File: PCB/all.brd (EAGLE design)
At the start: 45 x 45 mm, 119 parts, among them J1 ISP Programmer, J2 LIPO-BATTERY-CONNECTOR, J8 BL-HP20AUW2C, U1 ATTINY1634MLF20, U2 LM3671, U3 MPU-6050-1, U4 BQ51013B_RHL_20, U5 MCP73831, U6 CAT4139, U7 BQ51013B_RHL_20, U8 BQ51013B_RHL_20, U9 BQ51013B_RHL_20

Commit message: Component placement
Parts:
- moved R6 87.2 mm to (2.29, 24.7), turned to 90 degrees
- moved J2 84.2 mm to (4.37, 19.7), turned to 270 degrees
- moved U5 83.2 mm to (4.33, 24.3), turned to 0 degrees
- moved L2 77.9 mm to (21.6, 37.8), turned to 180 degrees
- moved C15 77.5 mm to (7.28, 23.1), turned to 90 degrees
- moved C12 74.8 mm to (11.4, 23.6), turned to 270 degrees
- moved R19 74.8 mm to (17.4, 11.8), turned to 90 degrees
- moved C10 74.8 mm to (15.2, 26.7), turned to 0 degrees
- moved R18 74.2 mm to (15.5, 14.9), turned to 90 degrees
- moved U2 73.5 mm to (22.0, 34.1), turned to 270 degrees
- moved R20 72.5 mm to (18.9, 11.8), turned to 270 degrees
- moved C13 72.5 mm to (17.4, 26.3), turned to 90 degrees
- moved C8 71.6 mm to (21.8, 32.0), turned to 0 degrees
- moved L1 71.4 mm to (23.8, 7.85), turned to 0 degrees
- moved U3 71.1 mm to (14.6, 22.9), turned to 180 degrees
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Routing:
- net RGB: track 0.00 -> 5.78 mm
- net 5V: track 5.39 -> 8.41 mm
- net N$15: track 0.00 -> 2.55 mm
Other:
- board text added: "Board layout 26.7.2016"
- board text added: "www.helentronica.com"
- board text removed: "Prelimirary board layout 26.7.2016"

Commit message: routing finished
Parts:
- C1, C17, C20, C22, C25, C28, C5, CP1, CP2, CP3, CP4, CP5, CP6, CP7, CP8, CS, CS1, CS10, CS11, CS12, CS13, CS14, CS15, CS16, CS17, CS19, CS2, CS20, CS21, CS22, CS23, CS24, CS25, CS26, CS27, CS28, CS29, CS3, CS30, CS31, CS32, CS33, CS34, CS35, CS36, CS37, CS38, CS39, CS4, CS5, CS6, CS7, CS8, CS9: device rcl:C0603 -> rcl:C0603K
- C10, C11, C12, C6, C7, C8, C9: device rcl:C0402 -> rcl:C0603K
- C13: device SparkFun:0603-CAP -> rcl:C0603K
- moved D2 4.85 mm to (8.58, 15.9)
- moved C1 3.25 mm to (17.2, 11.8)
- moved U5 1.97 mm to (5.93, 23.2)
- moved J2 1.51 mm to (4.57, 18.2)
- moved C15 1.35 mm to (8.63, 23.1)
- moved C14 1.25 mm to (36.3, 24.3)
- moved JP2 1.25 mm to (39.3, 20.5)
- moved R19 1.25 mm to (18.6, 11.8)
- moved R20 1.25 mm to (20.1, 11.8)
- moved R5 1.25 mm to (35.9, 20.5)
- moved R6 0.91 mm to (2.84, 25.4), turned to 0 degrees
- moved C5 0.88 mm to (24.1, 30.6)
- moved R1 0.46 mm to (26.3, 29.5)
- moved R15 0.35 mm to (8.15, 42.6)
- moved R4 0.35 mm to (42.6, 36.9)
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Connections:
- removed net VBAT: J2.P$1, U5.3
- net 5V: now also J2.P$1, U5.3
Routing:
- net V_QI_IN: track 3.32 -> 85.2 mm
- net 5V: track 8.41 -> 86.0 mm, vias 0 -> 3
- net 3.3V: track 23.8 -> 49.6 mm
- net SCL: track 6.12 -> 22.7 mm
- net N$18: track 0.00 -> 13.0 mm, vias 0 -> 2
- net PWM: track 0.00 -> 12.8 mm, vias 0 -> 1
- net N$64: track 0.00 -> 8.11 mm, vias 0 -> 1
- net SDA: track 13.2 -> 21.1 mm, vias 0 -> 1
- net N$2: track 0.00 -> 7.85 mm
- net N$63: track 0.00 -> 5.68 mm
- net N$65: track 0.00 -> 5.63 mm
- net N$3: track 0.00 -> 4.40 mm, vias 0 -> 1
- net RST: track 3.09 -> 7.10 mm
- net N$62: track 0.00 -> 3.49 mm
- net VBAT: track 2.66 -> 0.00 mm
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
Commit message: DRC done
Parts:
- added DRILEGEND: (no value), drilegend:DRILEGEND
- J3, J4, J5, J6: value (none) -> Qi coil
- J7: value (none) -> UART
- Q1, Q2: value (none) -> NPN
- R18: value (none) -> 1.8
- moved C11 0.78 mm to (13.5, 19.0)
- moved C8 0.46 mm to (21.6, 31.6)
- moved U2 0.20 mm to (22.0, 33.9)
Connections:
- net 5V renamed +5V
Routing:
- net GND: track 9.08 -> 67.8 mm, vias 2 -> 47
- net V_QI3: track 12.3 -> 14.2 mm
- net V_QI_IN: track 85.2 -> 86.5 mm
- net 3.3V: track 49.6 -> 50.6 mm
- net N$1: track 1.59 -> 2.37 mm

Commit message: gerber generated
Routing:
- net GND: vias 47 -> 49
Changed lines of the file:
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@@
 <layer number="14" name="Route14" color="1" fill="6" visible="no" active="no"/>
 <layer number="15" name="Route15" color="4" fill="6" visible="no" active="no"/>
-<layer number="16" name="Bottom" color="1" fill="1" visible="yes" active="yes"/>
+<layer number="16" name="Bottom" color="1" fill="1" visible="no" active="yes"/>
 <layer number="17" name="Pads" color="2" fill="1" visible="yes" active="yes"/>
 <layer number="18" name="Vias" color="2" fill="1" visible="yes" active="yes"/>
-<layer number="19" name="Unrouted" color="6" fill="1" visible="yes" active="yes"/>
+<layer number="19" name="Unrouted" color="6" fill="1" visible="no" active="yes"/>
 <layer number="20" name="Dimension" color="15" fill="1" visible="yes" active="yes"/>
 <layer number="21" name="tPlace" color="7" fill="1" visible="yes" active="yes"/>
-<layer number="22" name="bPlace" color="7" fill="1" visible="yes" active="yes"/>
+<layer number="22" name="bPlace" color="7" fill="1" visible="no" active="yes"/>
 <layer number="23" name="tOrigins" color="15" fill="1" visible="no" active="yes"/>
 <layer number="24" name="bOrigins" color="15" fill="1" visible="no" active="yes"/>
-<layer number="25" name="tNames" color="7" fill="1" visible="no" active="yes"/>
+<layer number="25" name="tNames" color="7" fill="1" visible="yes" active="yes"/>
 <layer number="26" name="bNames" color="7" fill="1" visible="no" active="yes"/>
 <layer number="27" name="tValues" color="7" fill="1" visible="no" active="yes"/>
 <layer number="28" name="bValues" color="7" fill="1" visible="no" active="yes"/>
-<layer number="29" name="tStop" color="7" fill="3" visible="no" active="yes"/>
+<layer number="29" name="tStop" color="7" fill="3" visible="yes" active="yes"/>
 <layer number="30" name="bStop" color="7" fill="6" visible="no" active="yes"/>
 <layer number="31" name="tCream" color="7" fill="4" visible="no" active="yes"/>
@@
 <layer number="39" name="tKeepout" color="4" fill="11" visible="no" active="yes"/>
 <layer number="40" name="bKeepout" color="1" fill="11" visible="no" active="yes"/>
-<layer number="41" name="tRestrict" color="4" fill="10" visible="yes" active="yes"/>
-<layer number="42" name="bRestrict" color="1" fill="10" visible="yes" active="yes"/>
+<layer number="41" name="tRestrict" color="4" fill="10" visible="no" active="yes"/>
+<layer number="42" name="bRestrict" color="1" fill="10" visible="no" active="yes"/>
 <layer number="43" name="vRestrict" color="2" fill="10" visible="no" active="yes"/>
 <layer number="44" name="Drills" color="7" fill="1" visible="no" active="yes"/>
 <layer number="45" name="Holes" color="7" fill="1" visible="no" active="yes"/>
 <layer number="46" name="Milling" color="3" fill="1" visible="no" active="yes"/>
-<layer number="47" name="Measures" color="7" fill="1" visible="yes" active="yes"/>
-<layer number="48" name="Document" color="7" fill="1" visible="yes" active="yes"/>
+<layer number="47" name="Measures" color="7" fill="1" visible="no" active="yes"/>
+<layer number="48" name="Document" color="7" fill="1" visible="no" active="yes"/>
 <layer number="49" name="Reference" color="7" fill="1" visible="no" active="yes"/>
 <layer number="50" name="dxf" color="7" fill="1" visible="no" active="no"/>
@@
 <layer number="131" name="tAdjust" color="7" fill="1" visible="no" active="yes"/>
 <layer number="132" name="bAdjust" color="7" fill="1" visible="no" active="yes"/>
-<layer number="144" name="DrillLegend" color="7" fill="1" visible="yes" active="yes"/>
+<layer number="144" name="DrillLegend" color="7" fill="1" visible="no" active="yes"/>
 <layer number="145" name="DrillLegend_01-16" color="2" fill="9" visible="no" active="yes"/>
 <layer number="146" name="DrillLegend_01-20" color="3" fill="9" visible="no" active="yes"/>
@@
 <text x="110" y="-55" size="2.54" layer="48">Pero</text>
 <text x="110" y="-60" size="2.54" layer="48">July, 2016</text>
-<dimension x1="40" y1="5" x2="40" y2="0" x3="40" y3="2.5" textsize="2.54" layer="47" dtype="vertical" extoffset="1" visible="yes"/>
 <text x="60" y="-55" size="2.54" layer="48">Board layout
 26.7.2016</text>
@@
 <text x="42.5" y="33.75" size="2.54" layer="26" rot="MR0">www.helentronica.com</text>
 <dimension x1="0" y1="45" x2="22.5" y2="42.5" x3="11.25" y3="48.75" textsize="2.54" layer="47" dtype="horizontal" visible="yes"/>
-<dimension x1="0" y1="0" x2="22.5" y2="2.5" x3="11.25" y3="-5.6" textsize="2.54" layer="47" dtype="horizontal" visible="yes"/>
-<dimension x1="0" y1="0" x2="2.5" y2="22.5" x3="-4.65" y3="11.25" textsize="2.54" layer="47" dtype="vertical" visible="yes"/>
+<dimension x1="0" y1="5" x2="22.5" y2="2.5" x3="11.25" y3="-5.6" textsize="2.54" layer="47" dtype="horizontal" visible="yes"/>
+<dimension x1="5" y1="0" x2="2.5" y2="22.5" x3="-4.65" y3="11.25" textsize="2.54" layer="47" dtype="vertical" visible="yes"/>
 <dimension x1="45" y1="0" x2="42.5" y2="22.5" x3="51.75" y3="11.25" textsize="2.54" layer="47" dtype="vertical" visible="yes"/>
 <wire x1="7.5" y1="20.508" x2="7.5" y2="19.492" width="0.1016" layer="145"/>
@@
 <wire x1="42.5" y1="21.992" x2="41.992" y2="22.5" width="0.1016" layer="146"/>
 <wire x1="41.992" y1="22.5" x2="42.5" y2="23.008" width="0.1016" layer="146"/>
+<dimension x1="21.51005" y1="41.51005" x2="23.48995" y2="43.48995" x3="23.48995" y3="43.48995" textsize="1.778" layer="47" dtype="diameter" visible="yes"/>
 </plain>
 <attributes>
@@
 <via x="26" y="3" extent="1-16" drill="0.3302"/>
 <via x="19" y="2" extent="1-16" drill="0.3302"/>
+<via x="10.55" y="26.55" extent="1-16" drill="0.3302"/>
+<via x="43" y="19" extent="1-16" drill="0.3302"/>
 <wire x1="35" y1="35.85" x2="35.425" y2="35.85" width="0" layer="19" extent="1-1"/>
 <wire x1="35.425" y1="34.35" x2="35.4" y2="34.35" width="0" layer="19" extent="1-1"/>
@@
 <wire x1="13.83165" y1="21.74745" x2="14" y2="22.5" width="0" layer="19" extent="1-1"/>
 <wire x1="38" y1="10.175" x2="35.85" y2="9.85" width="0" layer="19" extent="1-1"/>
-<wire x1="19" y1="2" x2="26" y2="3" width="0" layer="19" extent="1-1"/>
 </signal>
 <signal name="3.3V">
@@
 <contactref element="CP2" pad="2"/>
 <contactref element="CS7" pad="2"/>
-<polygon width="0" layer="1" thermals="no">
+<polygon width="0.0254" layer="1" thermals="no">
 <vertex x="33.25" y="39.65"/>
 <vertex x="33.25" y="37.35"/>
@@
 <contactref element="CP4" pad="2"/>
 <contactref element="CS17" pad="2"/>
-<polygon width="0" layer="1" thermals="no">
+<polygon width="0.0254" layer="1" thermals="no">
 <vertex x="11.8" y="5.3"/>
 <vertex x="11.8" y="7.7"/>
@@
 <contactref element="CP6" pad="2"/>
 <contactref element="CS27" pad="2"/>
-<polygon width="0" layer="1" thermals="no">
+<polygon width="0.0254" layer="1" thermals="no">
 <vertex x="39.45" y="11.25"/>
 <vertex x="37.15" y="11.25"/>
@@
 <contactref element="CP8" pad="2"/>
 <contactref element="CS37" pad="2"/>
-<polygon width="0" layer="1" thermals="no">
+<polygon width="0.0254" layer="1" thermals="no">
 <vertex x="5.35" y="33.25"/>
 <vertex x="7.7" y="33.25"/>
 <vertex x="7.7" y="28.7"/>
 <vertex x="6.4" y="28.7"/>
-<vertex x="6.4" y="26.7"/>
-<vertex x="5.3" y="26.7"/>
+<vertex x="6.4" y="26.65"/>
+<vertex x="5.35" y="26.65"/>
 </polygon>
 <wire x1="11.625" y1="35.9" x2="11.625" y2="34.675" width="0.3048" layer="1"/>

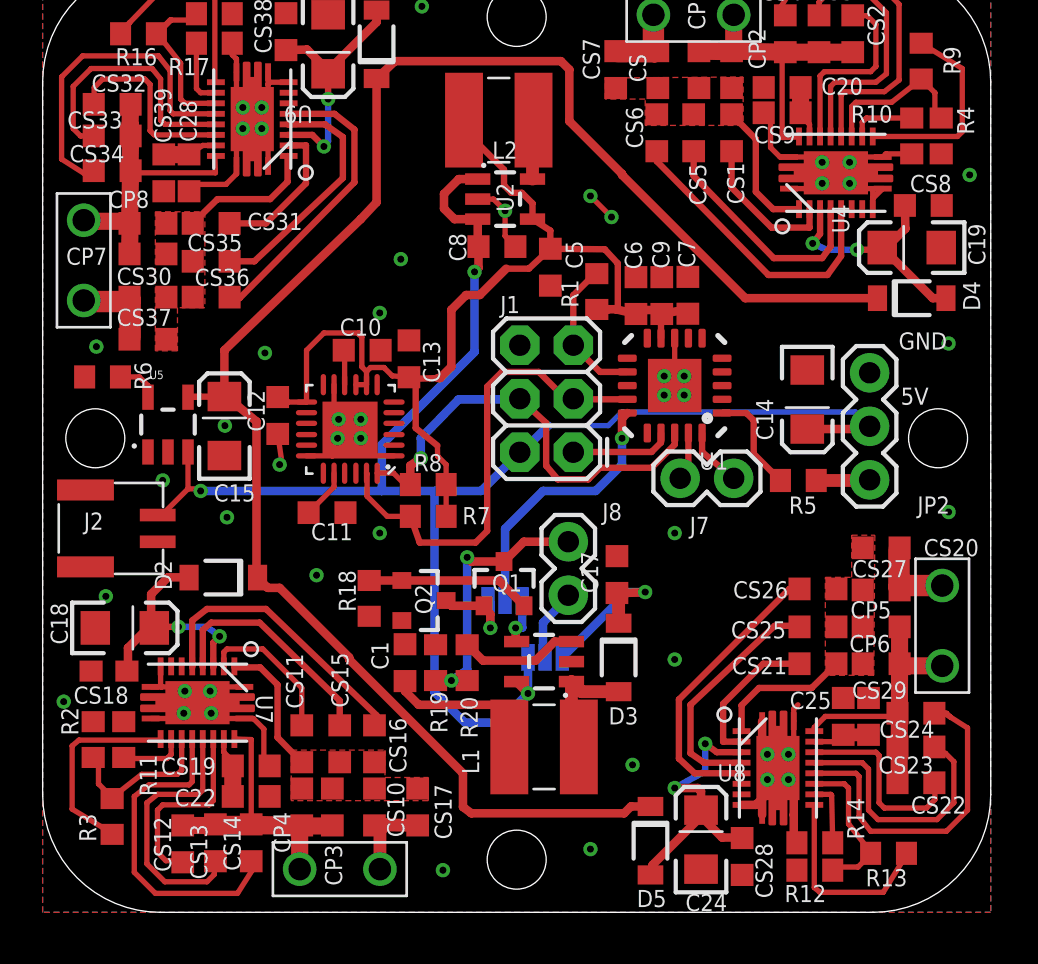
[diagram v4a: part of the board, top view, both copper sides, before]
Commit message: improved spacing, added silkscreen
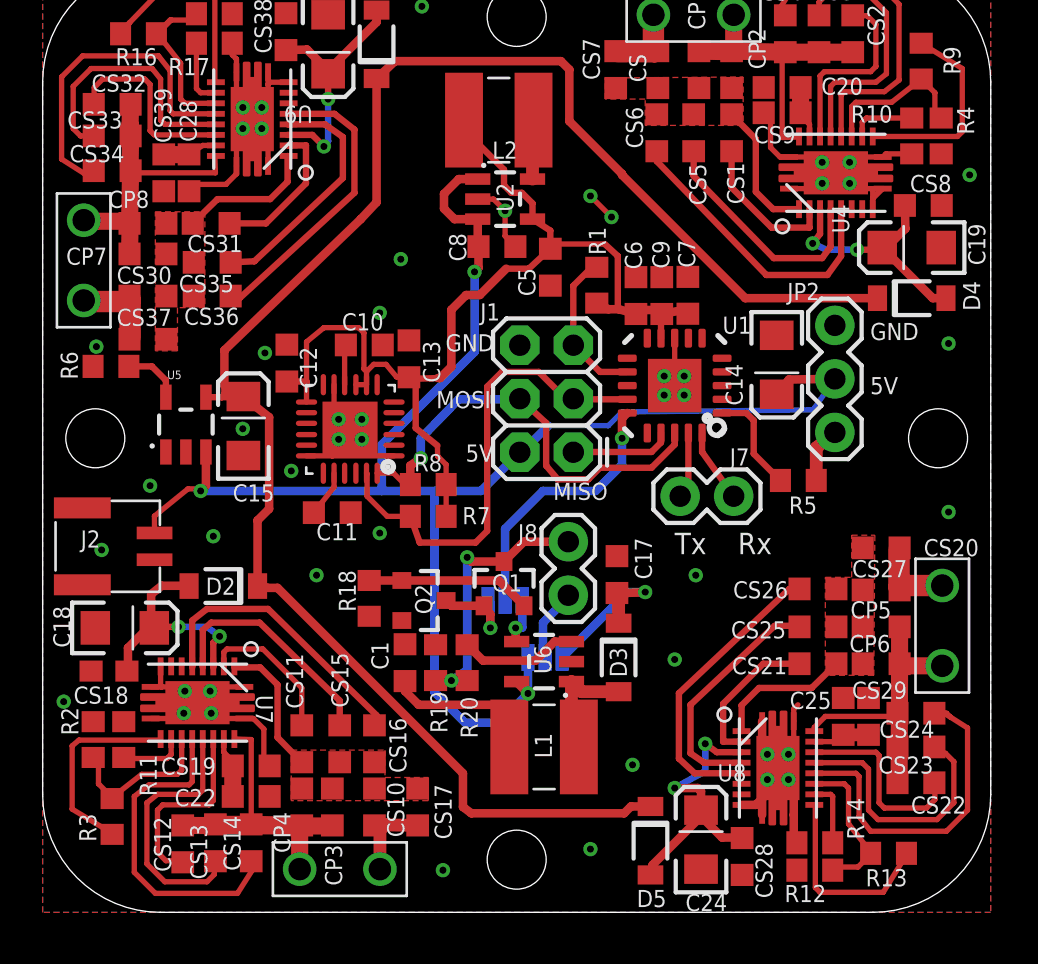
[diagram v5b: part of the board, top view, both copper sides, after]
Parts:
- moved JP2 2.79 mm to (37.6, 22.8)
- moved C12 2.53 mm to (11.6, 26.1), turned to 90 degrees
- moved C14 2.20 mm to (34.8, 26.0)
- moved C15 0.90 mm to (9.53, 23.1)
- moved J2 0.86 mm to (4.42, 17.4)
- moved J7 0.85 mm to (32.8, 19.8)
- moved U5 0.85 mm to (6.80, 23.1)
- moved R6 0.64 mm to (3.24, 25.9)
- moved D2 0.40 mm to (8.58, 15.5)
- moved R1 0.30 mm to (26.3, 29.8)
- moved C10 0.27 mm to (15.3, 26.9)
- moved C11 0.25 mm to (13.7, 19.0)
- moved CS36 0.07 mm to (8.05, 29.2)
- moved CS35 0.07 mm to (8.05, 30.9)
- moved CS30 0.05 mm to (5.00, 29.2)
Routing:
- net V_QI_IN: track 86.5 -> 84.2 mm
- net GND: track 67.8 -> 66.5 mm
- net TX: track 2.26 -> 3.24 mm
- net 3.3V: track 50.6 -> 51.4 mm
- net N$17: track 2.03 -> 2.83 mm
- net RX: track 2.85 -> 3.48 mm
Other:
- board text added: "MISO"
- board text added: "MOSI"
- board text added: "Rx"
- board text added: "Tx"
